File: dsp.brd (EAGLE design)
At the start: 190 x 112.4 mm, 117 parts, among them IC1 OPA2134P, IC2 OPA2134P, Q1 BC550B, U1 STM32F405RGT6, U2 CODECODER-WM8731SEDS/V(SSOP28), U4 LM2575HVS-3.3/NOPB, X1 ABLS-8.000MHZ-B4-T

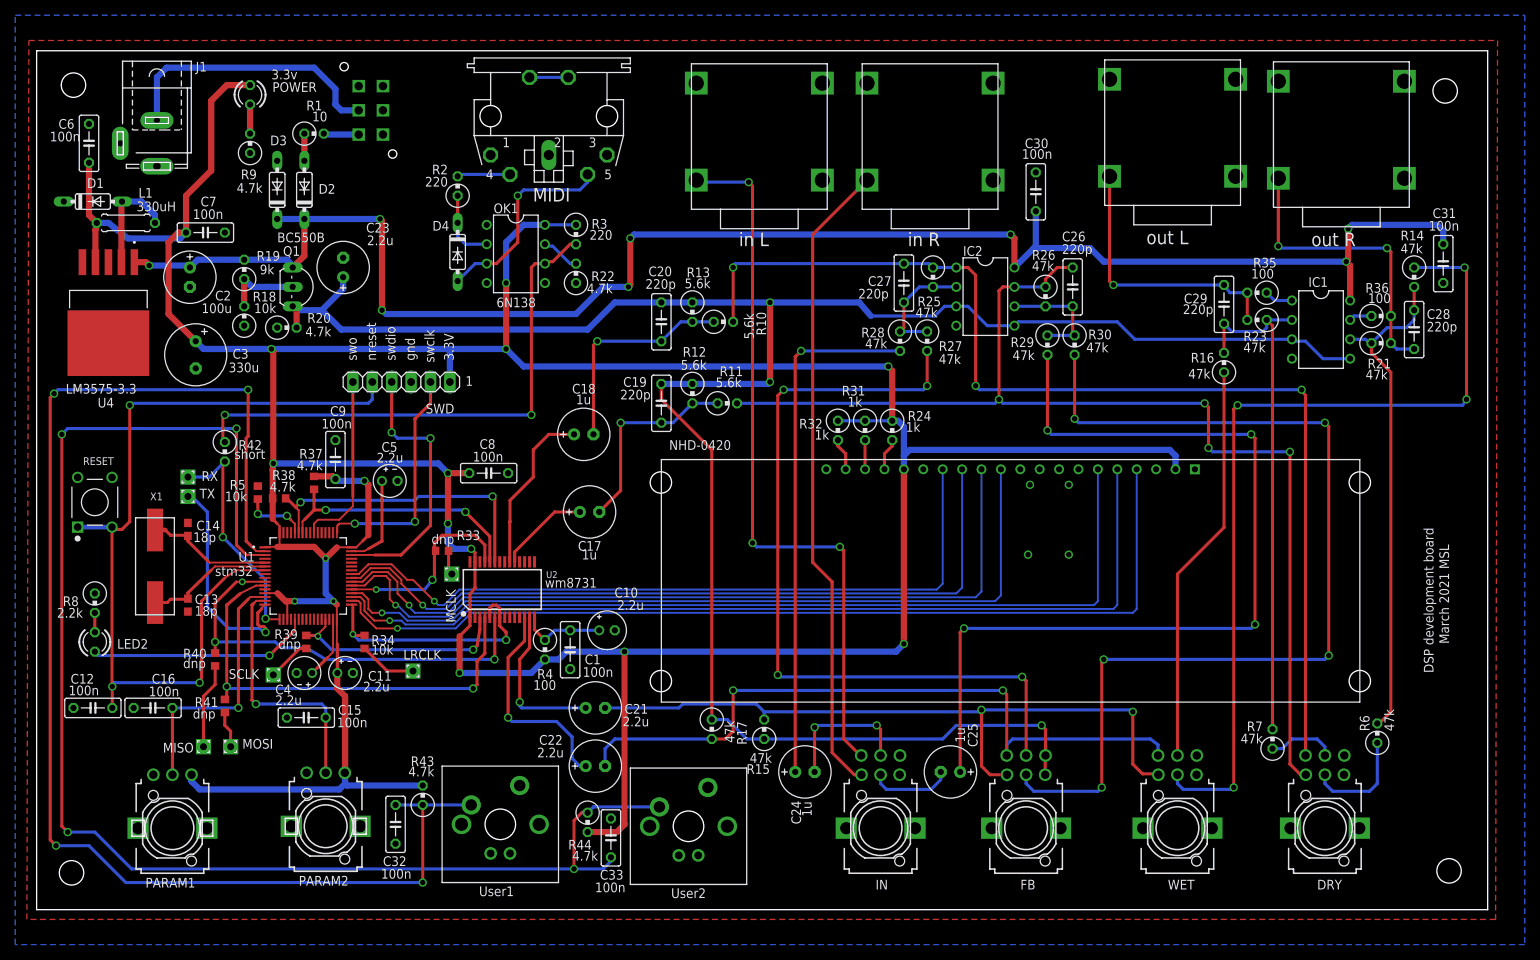
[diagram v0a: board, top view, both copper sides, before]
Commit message: fixed mclk and uart connections
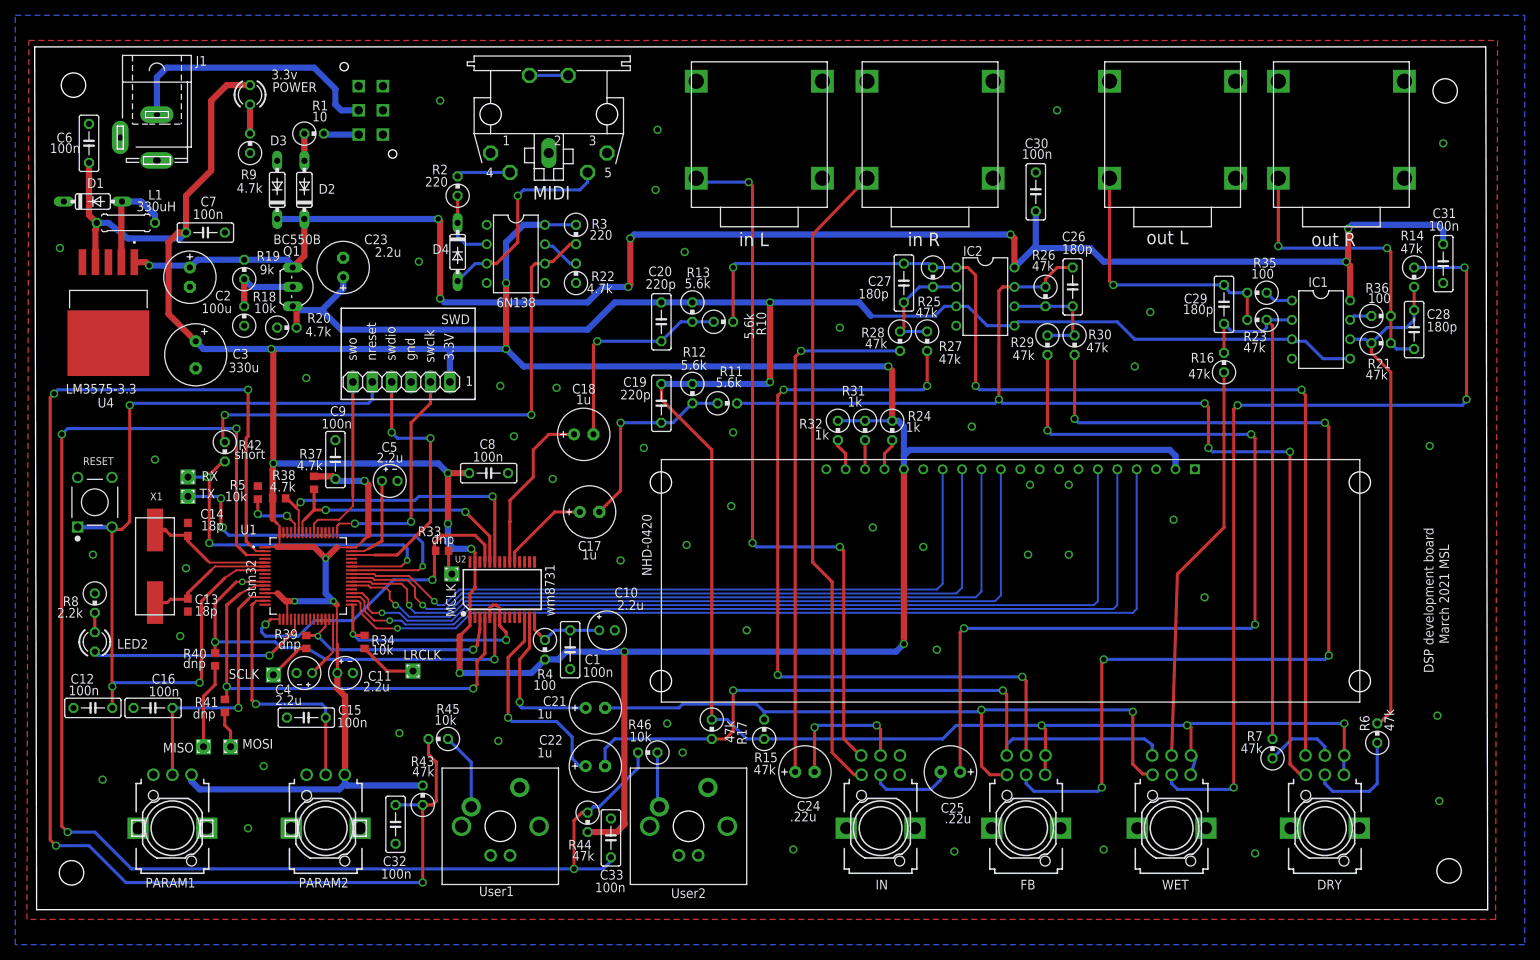
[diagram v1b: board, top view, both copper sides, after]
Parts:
- added R45, R46: 10k, dan:0309V
- C21, C22: value 2.2u -> 1u
- C24, C25: value 1u -> .22u
- C26, C27, C28, C29: value 220p -> 180p
- R43, R44: value 4.7k -> 47k
- moved R7 1.27 mm to (161.8, 21.1)
- moved J1 0.76 mm to (15.7, 101.1)
- moved WET 0.76 mm to (148.6, 10.7)
- moved MIDI 0.25 mm to (67.1, 104.1)
- moved OUTL 0.25 mm to (157.0, 95.8)
- moved PARAM2 0.25 mm to (37.8, 10.7)
- moved U$3 0.25 mm to (60.7, 10.9)
- moved INL 0.25 mm to (102.9, 95.8)
- moved INR 0.25 mm to (125.2, 95.8)
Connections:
- new net N$51: R45.1, U$3.SW1
- new net N$52: R46.1, U$4.SW1
- net 4.5V: now also DRY.1, DRY.4, WET.1, WET.4
- net GND: no longer DRY.1, DRY.4, WET.1, WET.4
- net MCLK: now also U1.17; no longer U1.37
- net N$50: now also U1.43; no longer U1.17
- net N$8: now also U1.42; no longer U1.16
- net SWITCH1: now also R45.2; no longer U$3.SW1
- net SWITCH2: now also R46.2; no longer U$4.SW1
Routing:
- net 4.5V: track 277.3 -> 331.4 mm, vias 3 -> 5
- net N$50: track 30.9 -> 49.8 mm, vias 2 -> 3
- net N$8: track 29.5 -> 48.1 mm, vias 1 -> 3
- net MCLK: track 26.5 -> 44.2 mm
- net N$51: track 0.00 -> 10.2 mm
- net N$52: track 0.00 -> 7.22 mm
- net SWITCH1: track 178.3 -> 182.5 mm
- net 9V: track 224.7 -> 222.6 mm
- net DB4: track 106.9 -> 105.0 mm
- net SWITCH2: track 187.4 -> 188.7 mm
- net N$18: track 68.3 -> 69.5 mm
- net DB7: track 96.3 -> 95.2 mm
- net DB5: track 103.4 -> 102.5 mm
- net N$37: track 36.1 -> 35.3 mm
- net N$21: track 113.6 -> 114.3 mm
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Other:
- board size 190 x 112.4 mm -> 190.2 x 113 mm

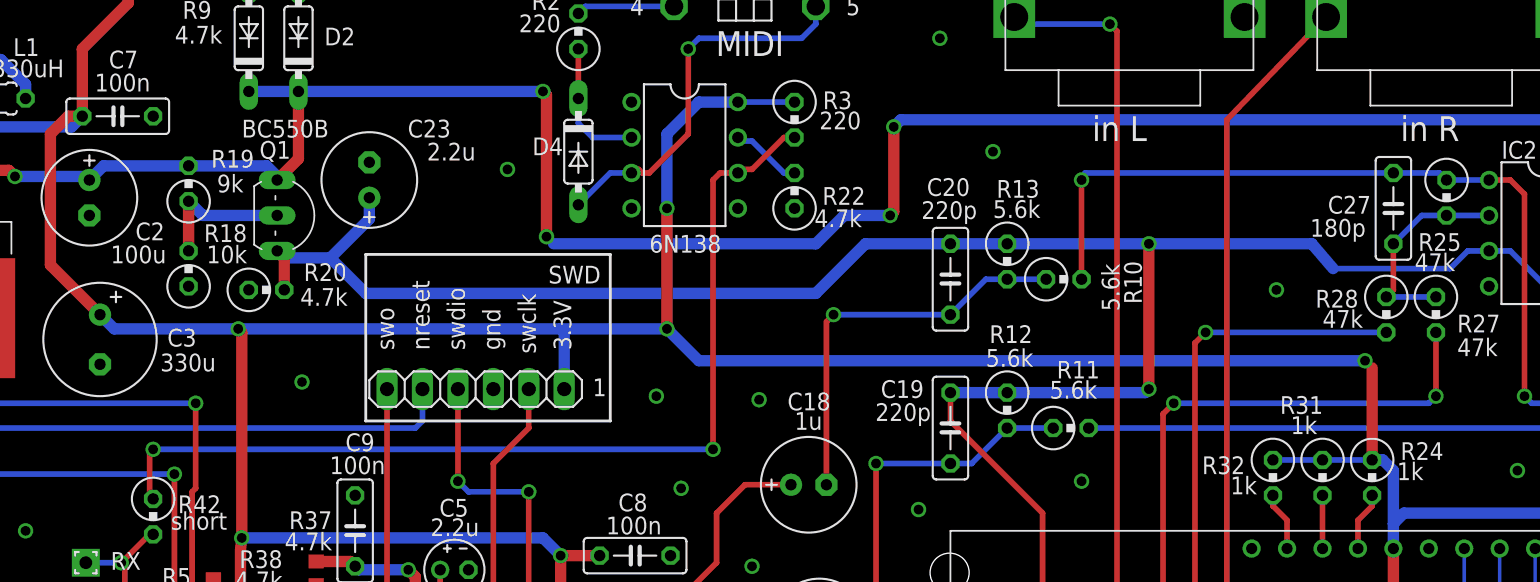
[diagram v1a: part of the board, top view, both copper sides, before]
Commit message: changed virtual ground to an op amp buffer
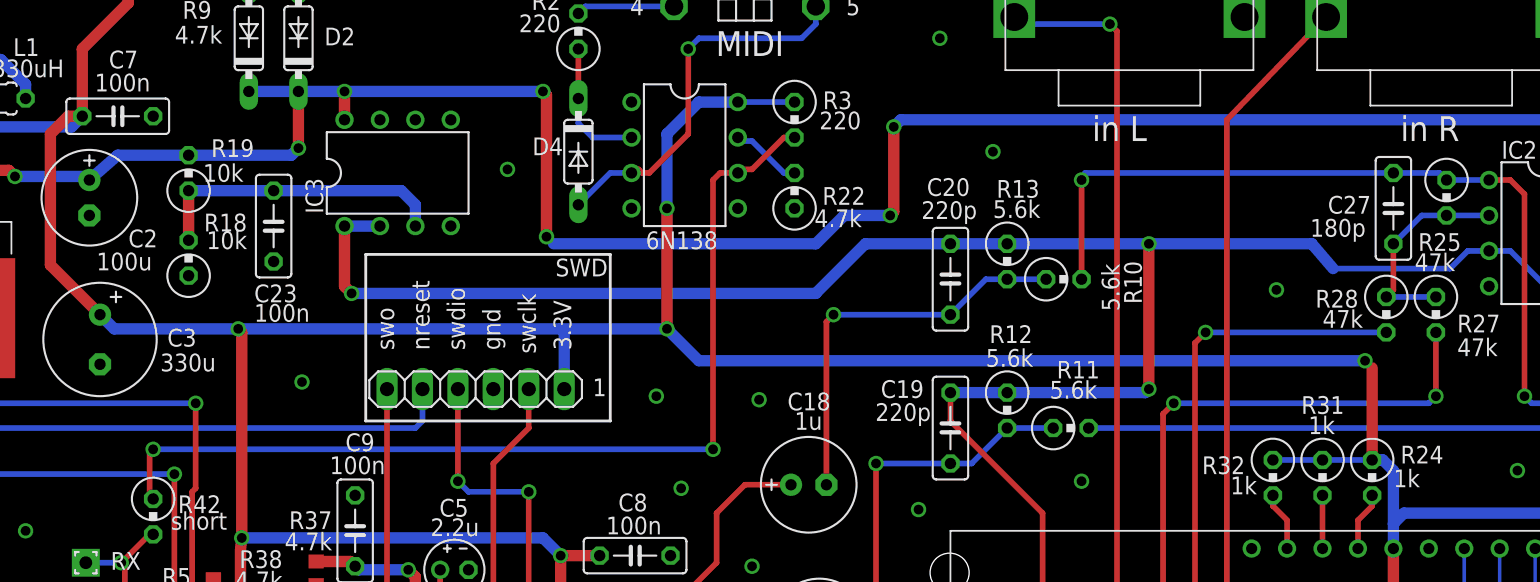
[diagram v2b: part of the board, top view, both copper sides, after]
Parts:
- removed Q1: BC550B, dan:TO92-EBC
- removed R20: 4.7k, dan:0309V
- added IC3: OPA2134P, dan:DIL08
- C23: value 2.2u -> 100n; device dan:E2,5-7 -> dan:C050-025X075
- R19: value 9k -> 10k
- moved C23 7.61 mm to (33.3, 80.8), turned to 270 degrees
- moved R18 0.76 mm to (27.2, 78.5)
- moved R19 0.76 mm to (27.2, 84.6)
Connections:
- net 4.5V: now also IC3.1, IC3.2; no longer C23.+, Q1.E, R20.2
- net 9V: now also IC3.8; no longer Q1.C
- net GND: now also C23.2, IC3.4; no longer C23.-, R20.1
- net N$20: now also C23.1, IC3.3; no longer Q1.B
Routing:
- net N$20: track 10.3 -> 21.8 mm
- net 4.5V: track 331.4 -> 323.9 mm, vias 5 -> 6
- net 9V: track 222.6 -> 223.1 mm, vias 8 -> 10

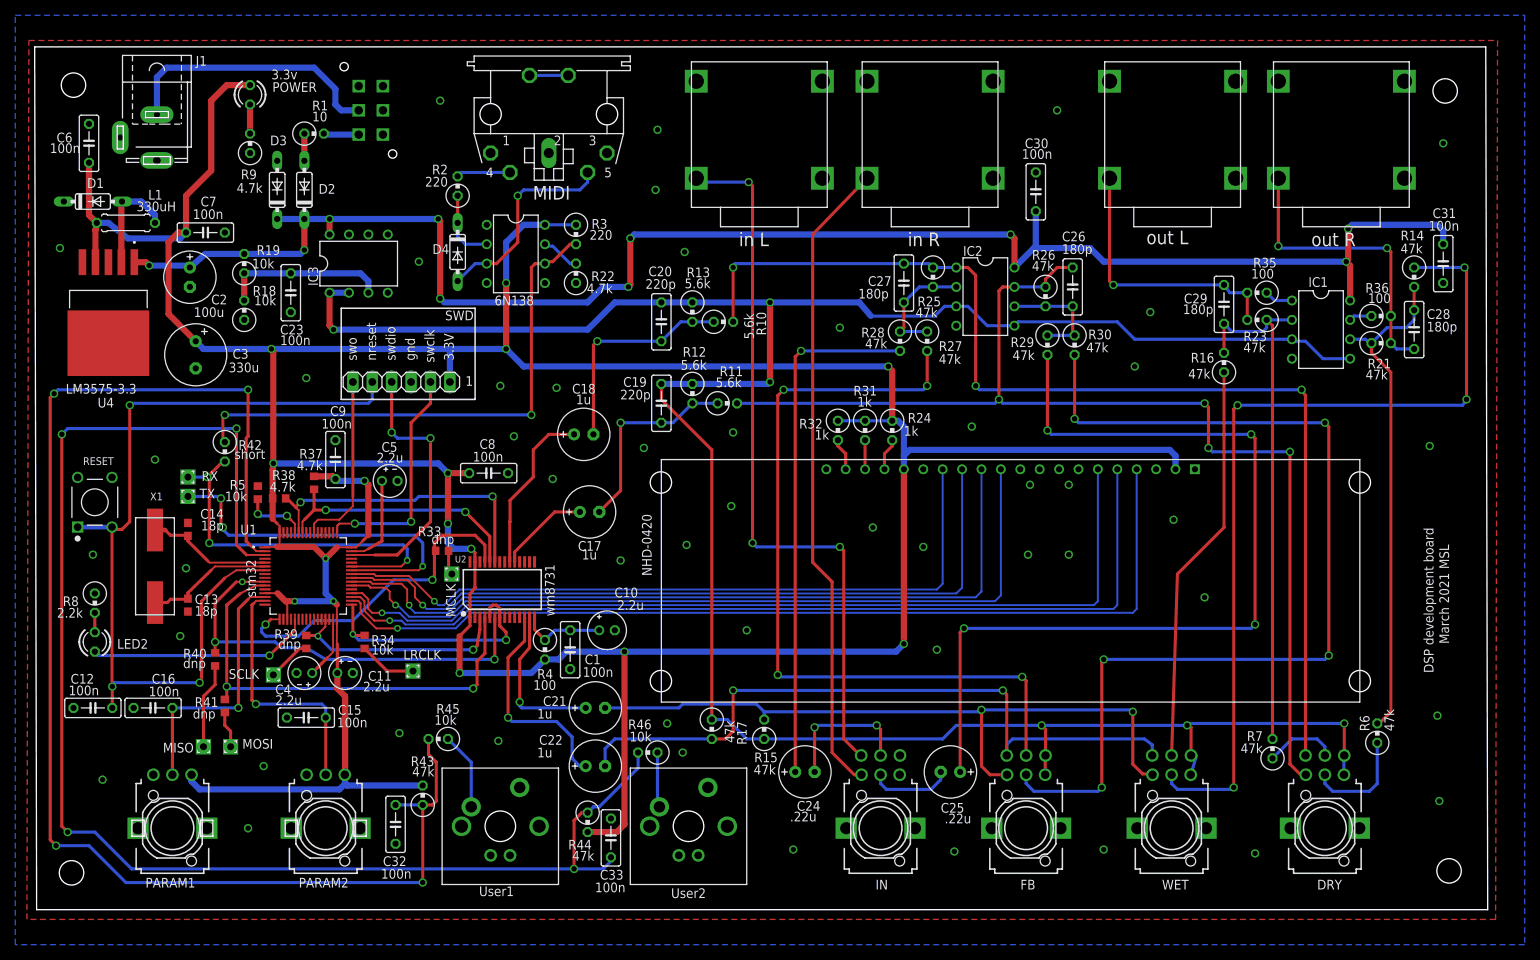
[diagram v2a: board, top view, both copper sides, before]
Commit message: mono routing, ac coupled op, jumper for feedback
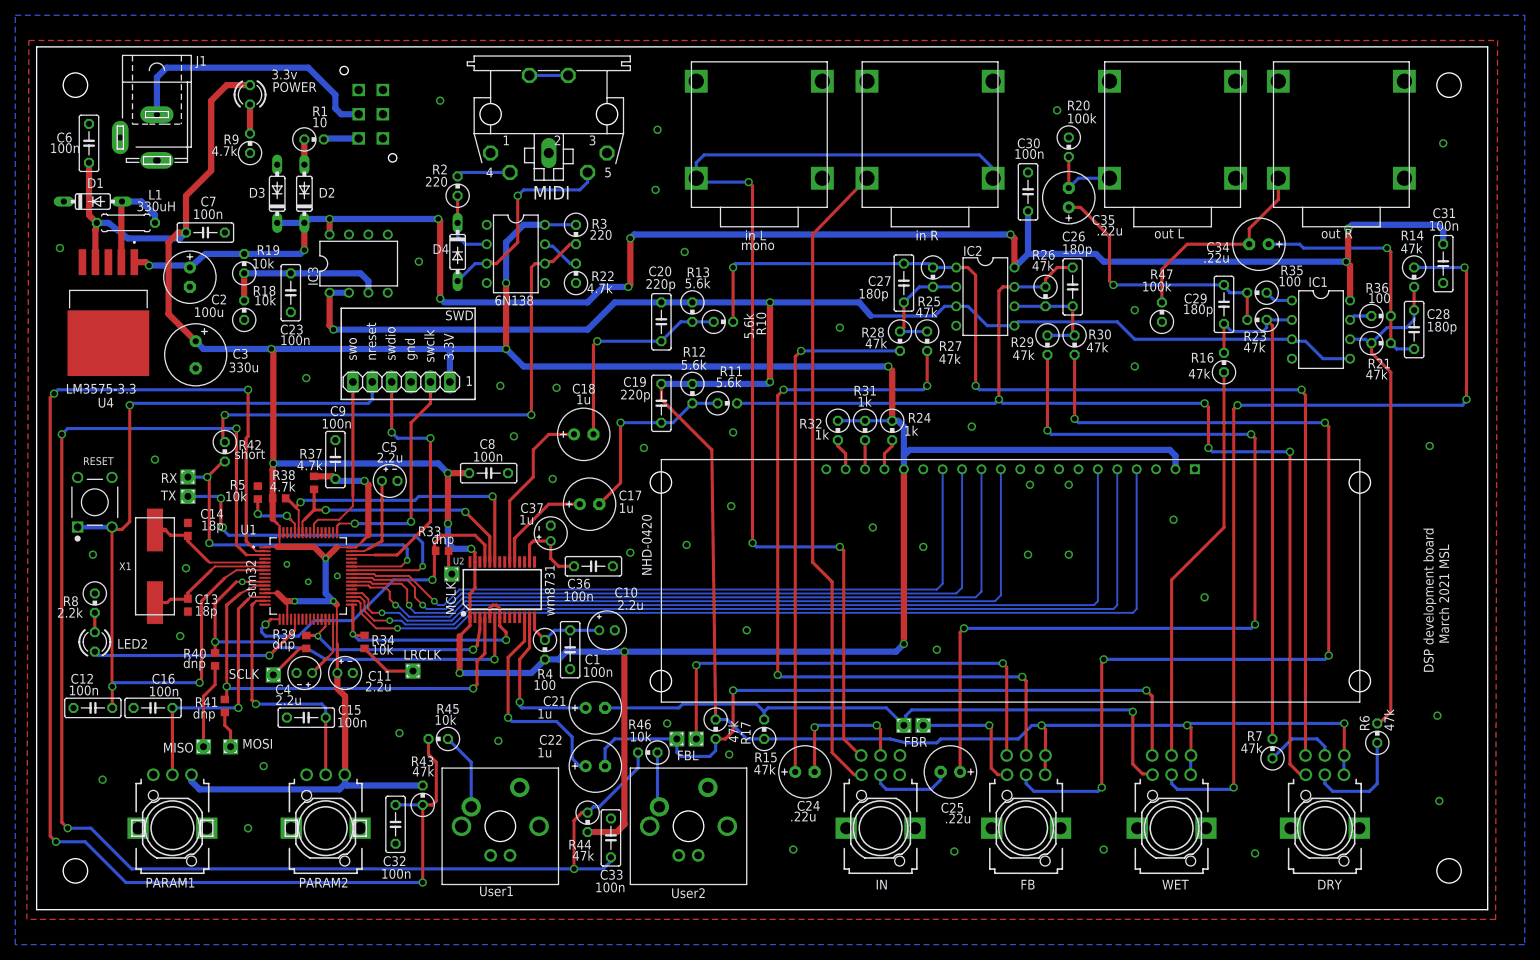
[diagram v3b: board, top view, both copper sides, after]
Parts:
- added C34, C35: .22u, dan:E2,5-7
- added C36: 100n, dan:C050-025X075
- added C37: 1u, dan:E2-4
- added FBL, FBL1, FBR, FBR1: (no value), synthdiy:2,0/0,9-S
- added R20, R47: 100k, dan:0309V
- moved C17 1.02 mm to (72.4, 53.1)
- moved C30 1.02 mm to (129.8, 94.0)
- moved R1 0.76 mm to (36.3, 100.8)
- moved R17 0.51 mm to (88.9, 23.6)
- moved D2 0.51 mm to (35.1, 93.7)
- moved D3 0.51 mm to (31.5, 93.7)
- moved U$2 0.51 mm to (43.4, 104.1)
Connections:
- removed net N$25: IN.6, INL.P$4
- new net N$53: C35.-, OUTL.P$4, R20.2
- new net N$54: C34.-, OUTR.P$4, R47.2
- new net N$55: FB.6, FBL1.1
- new net N$56: FB.3, FBR1.1
- new net N$57: C36.1, C37.+, U2.16
- new net N$58: IN.6, INL.P$4, INR.P$1
- net FBL: now also FBL.1; no longer FB.6
- net FBR: now also FBR.1; no longer FB.3
- net GND: now also C36.2, C37.-, OUTL.P$2, OUTR.P$2, R20.1, R47.1; no longer INR.P$1
- net N$23: now also C34.+; no longer OUTR.P$4
- net N$24: now also C35.+; no longer OUTL.P$4
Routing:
- net N$58: track 0.00 -> 138.0 mm, vias 0 -> 3
- net N$25: track 94.8 -> 0.00 mm, vias 3 -> 0
- net N$55: track 0.00 -> 62.2 mm, vias 0 -> 2
- net N$54: track 0.00 -> 27.3 mm
- net N$56: track 0.00 -> 16.8 mm, vias 0 -> 1
- net N$57: track 0.00 -> 11.0 mm
- net FBR: track 94.6 -> 84.7 mm, vias 2 -> 1
- net N$53: track 0.00 -> 9.92 mm
- net N$23: track 39.2 -> 31.7 mm, vias 2 -> 1
- net RIN: track 12.0 -> 13.5 mm
- net 9V: track 223.1 -> 222.1 mm
- net N$15: track 26.6 -> 25.6 mm
- net 4.5V: track 323.9 -> 322.9 mm
- net N$24: track 35.8 -> 35.1 mm
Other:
- board size 190.2 x 113 mm -> 190 x 113 mm
- board text added: "mono"
